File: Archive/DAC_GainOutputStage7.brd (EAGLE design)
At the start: 110 x 110.3 mm, 78 parts, among them J1 1935190, J3 SJ-63033A, U1 LM317MQDCYR, U2 LM317MQDCYR

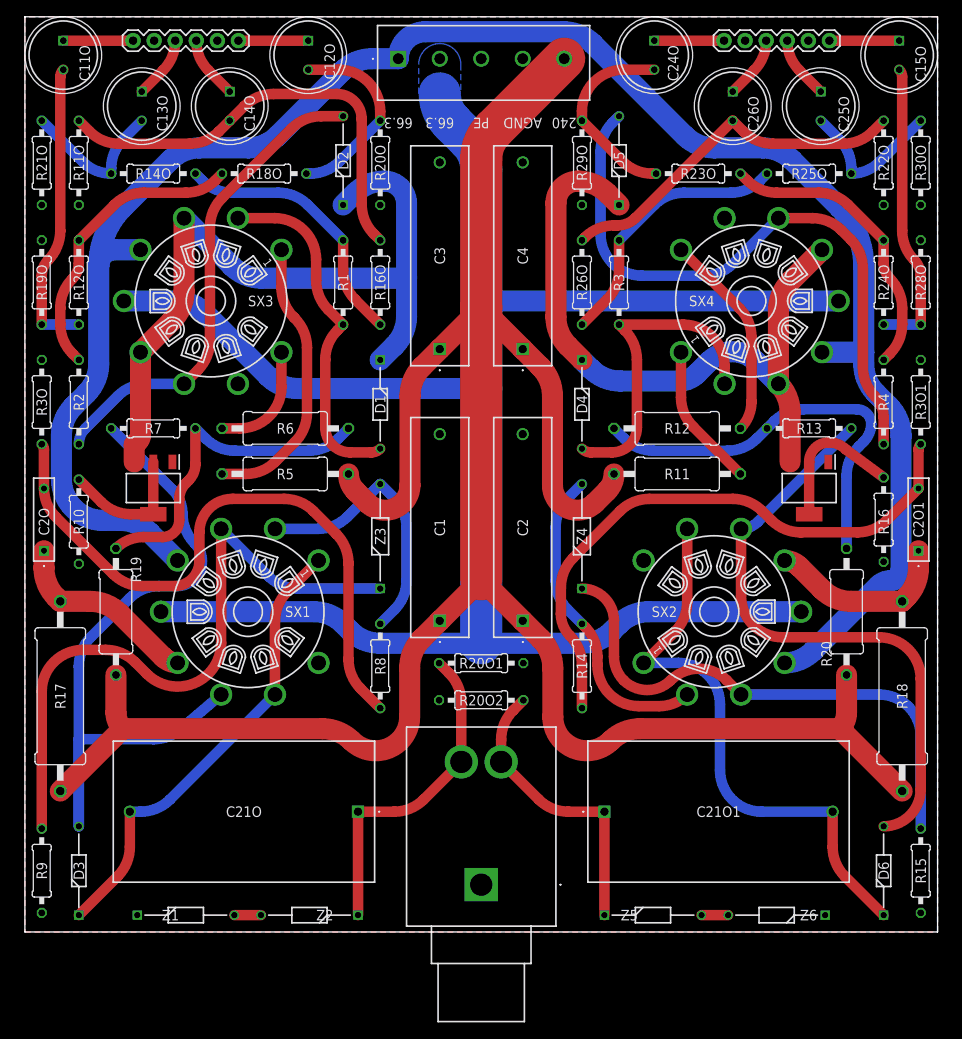
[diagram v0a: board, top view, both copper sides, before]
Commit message: Preliminary update complete for new tube
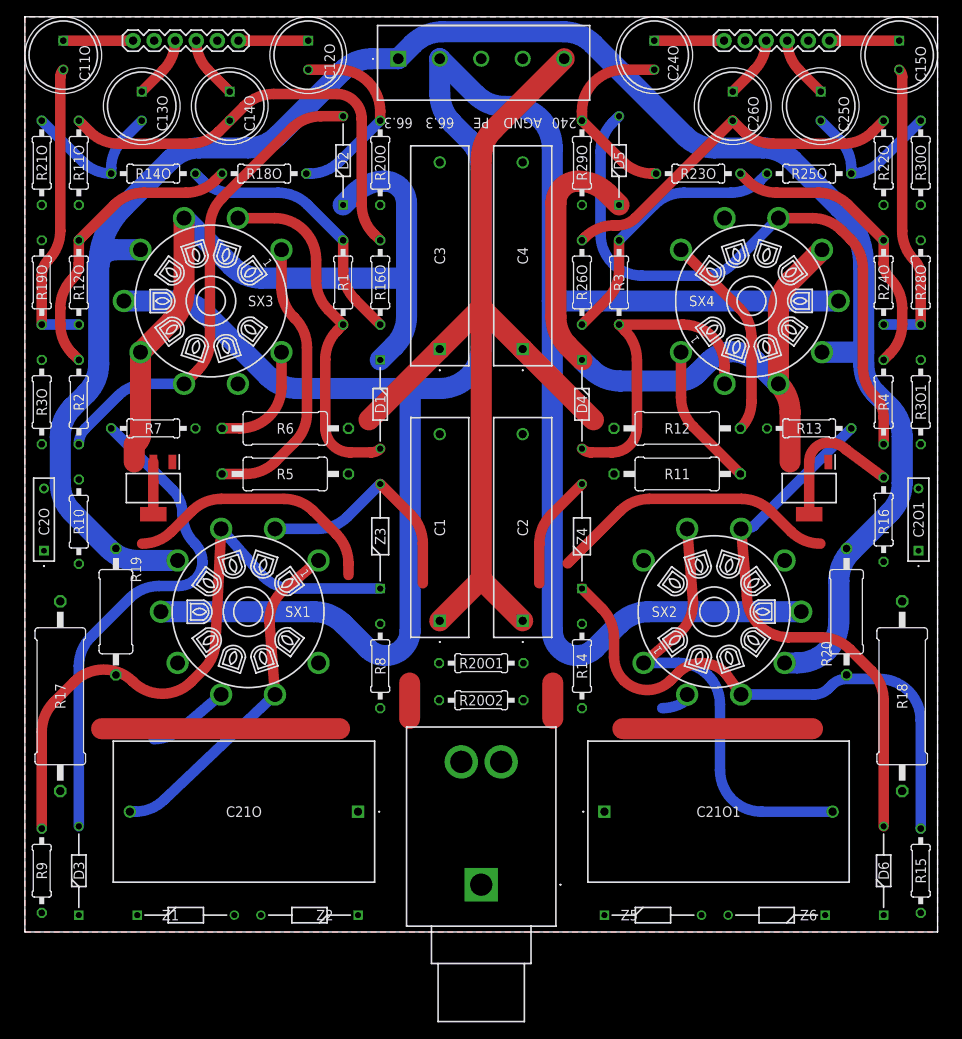
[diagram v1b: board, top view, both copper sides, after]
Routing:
- net +240VDC: track 280.6 -> 179.0 mm
- net 66.3VAC/2: track 236.7 -> 288.6 mm
- net N$9: track 49.7 -> 0.00 mm
- net N$16: track 76.4 -> 31.7 mm
- net N$1: track 40.3 -> 0.00 mm
- net R_OUT: track 39.8 -> 0.00 mm
- net N$17: track 71.5 -> 35.0 mm
- net L_OUT: track 35.3 -> 0.00 mm
- net N$39: track 23.3 -> 0.00 mm
- net N$40: track 22.3 -> 0.00 mm
- net N$14: track 37.4 -> 18.2 mm
- net N$23: track 88.1 -> 69.7 mm
- net N$18: track 55.7 -> 41.4 mm
- net N$3: track 67.6 -> 53.4 mm
- net N$37: track 16.7 -> 6.30 mm
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- removed copper zone on layer 16, net 66.3VAC/2

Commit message: Progress
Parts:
- removed R12, R6: 3k, Dual Mono Amp Library:0411/15
- R11, R5: value 18k -> 15k
- R15, R9: value 698 -> 249
- R17, R18: value 1k -> 402
- U1, U2: value LM317MQDCYR -> LM317MTG; device Dual Mono Amp Library:SOT230P700X180-4N -> Dual Mono Amp Library:TO254P482X997X2018-3P
- moved R19 30.1 mm to (31.4, 55.7), turned to 0 degrees
- moved R20 30.1 mm to (78.6, 55.7), turned to 0 degrees
- moved SX2 4.76 mm to (87.8, 33.6)
- moved SX1 4.72 mm to (22.2, 33.6)
- moved U2 2.58 mm to (92.0, 49.0), turned to 0 degrees
- moved U1 2.58 mm to (12.9, 49.0), turned to 0 degrees
- moved R11 1.25 mm to (78.6, 49.0)
- moved R5 1.25 mm to (31.4, 49.0)
- moved R19O 1.00 mm to (1.03, 73.3)
- moved R21O 1.00 mm to (1.03, 87.7)
- moved R3O 1.00 mm to (1.03, 58.9)
- moved R9 1.00 mm to (1.03, 2.38)
- moved C2O1 1.00 mm to (108.7, 40.9)
- moved R15 1.00 mm to (109.0, 2.38)
- moved R28O 1.00 mm to (109.0, 73.3)
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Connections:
- removed net N$43: R6.1, SX3.9
- removed net N$44: R12.1, SX4.9
- net N$1: now also SX3.6; no longer R6.2
- net N$22: now also SX3.8; no longer SX3.6
- net N$37: no longer U1.4
- net N$38: no longer U2.4
- net N$7: now also SX4.8; no longer SX4.6
- net N$9: now also SX4.6; no longer R12.2
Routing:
- net +240VDC: track 179.0 -> 279.9 mm
- net 66.3VAC/2: track 288.6 -> 247.8 mm
- net R_OUT: track 0.00 -> 39.8 mm
- net L_OUT: track 0.00 -> 35.3 mm
- net N$17: track 35.0 -> 69.2 mm
- net N$16: track 31.7 -> 64.7 mm
- net N$9: track 0.00 -> 27.3 mm
- net N$14: track 18.2 -> 43.6 mm
- net N$44: track 25.0 -> 0.00 mm
- net N$39: track 0.00 -> 19.6 mm
- net N$40: track 0.00 -> 18.3 mm
- net N$1: track 0.00 -> 16.3 mm
- net N$18: track 41.4 -> 57.0 mm
- net N$43: track 13.4 -> 0.00 mm
- net N$3: track 53.4 -> 66.0 mm
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- added copper zone on layer 16, net 66.3VAC/2
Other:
- board size 110 x 110.3 mm -> 112 x 110.3 mm
